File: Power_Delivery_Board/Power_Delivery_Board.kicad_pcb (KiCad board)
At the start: 2 copper layers, 36 parts, among them IC1 STUSB4500QTR, J1 USB C, J2 IO pins, J3 Power Output, J4 IO Pins, J5 Qwiic, Q1 STL6P3LLH6, SW1 SW_Push

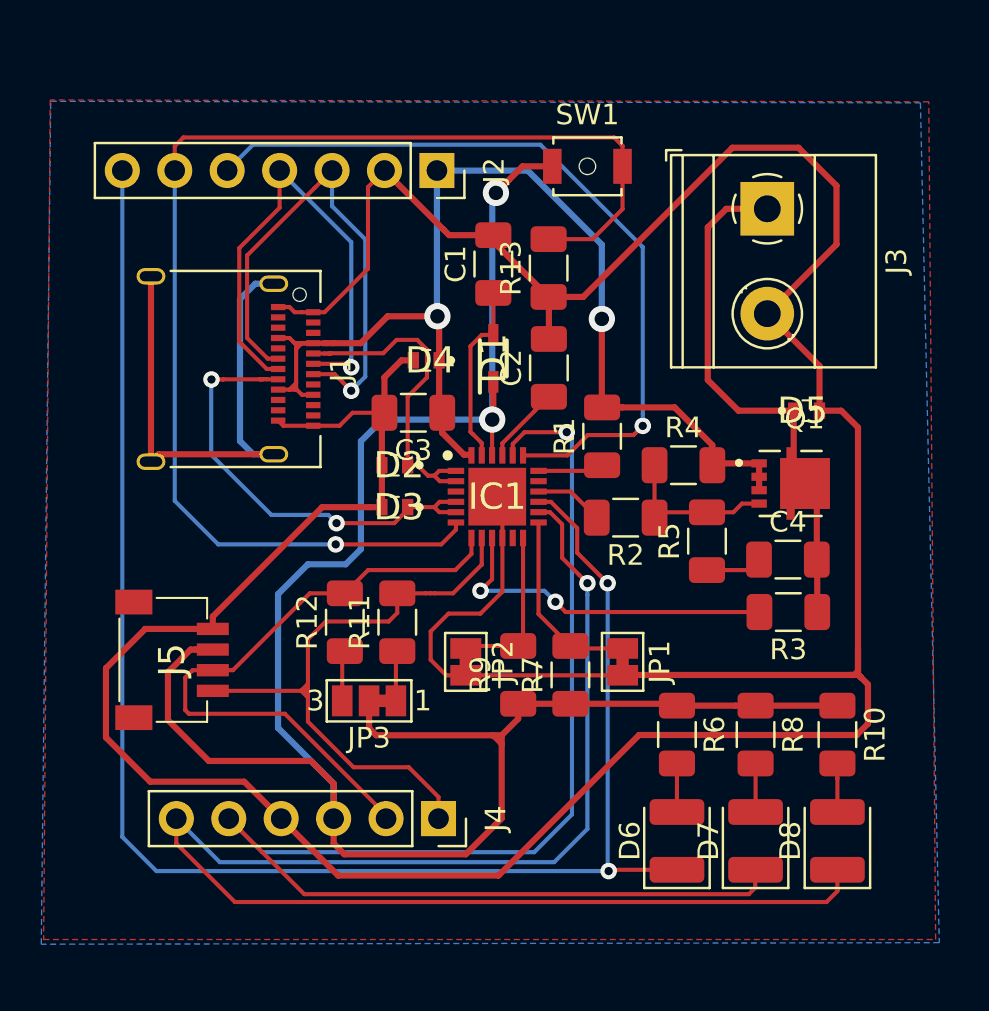
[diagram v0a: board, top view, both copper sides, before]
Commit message: Corrección de errores marcados por Fabiola
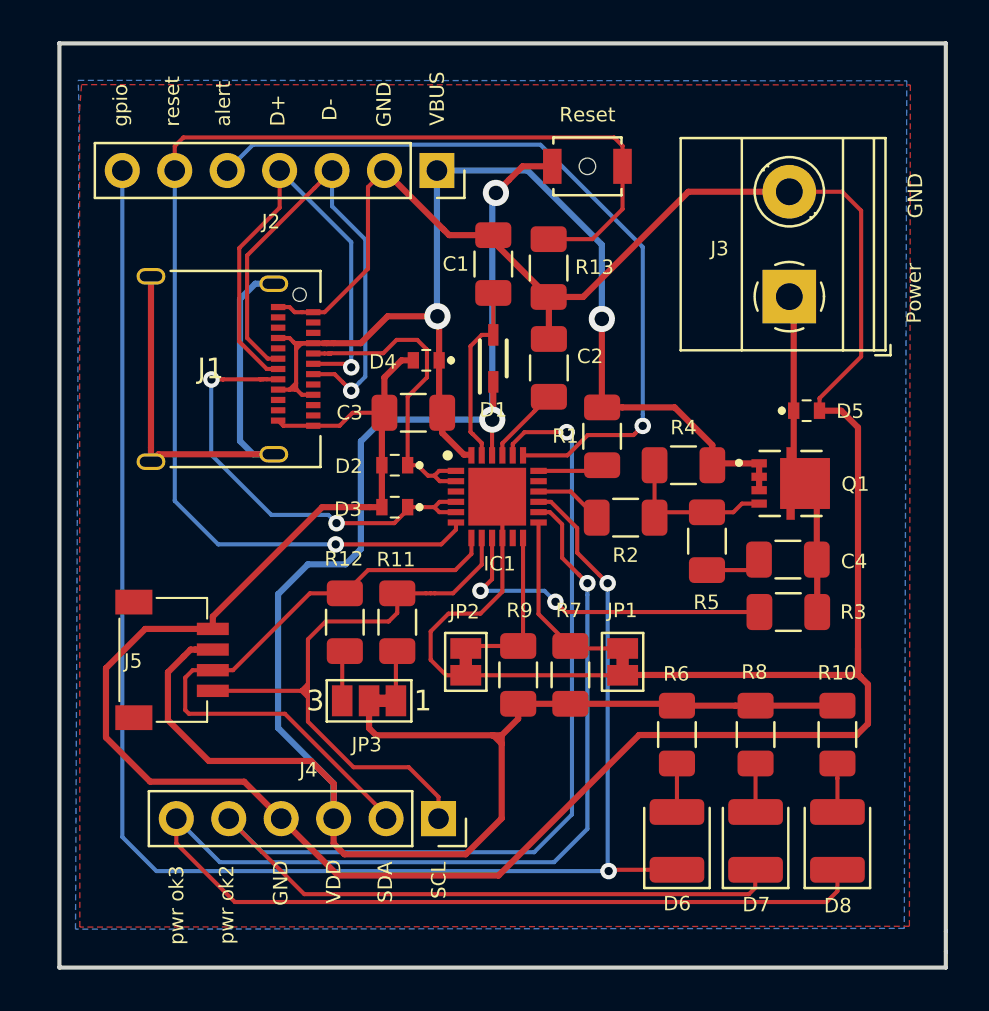
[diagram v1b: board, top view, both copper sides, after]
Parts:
- IC1: value STUSB4500QTR -> STUSB4500
- moved J3 4.39 mm to (168.6, 89.8), turned to 90 degrees
- renumbered SW1 to Reset
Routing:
- net power_output: track 25.7 -> 15.8 mm
- net GND: track 180.0 -> 177.2 mm
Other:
- board outline added: 43 x 44.8 mm
- board text added: "(por defecto) - pads 0.8mm - agujeros 0.4mm (VCC VDD GND) -pads 1.27 - agujeros 0.7mm"
- board text added: "D+"
- board text added: "D-"
- board text added: "GND"
- board text added: "Power"
- board text added: "SCL"
- board text added: "SDA"
- board text added: "Se utilizaron las capacidades del fabricante Ernesto Mayer (documentación en la raíz del proyecto)"
- board text added: "VBUS"
- board text added: "VDD"
- board text added: "alert"
- board text added: "gpio"
- board text added: "pistas (por defecto) - ancho 0.2mm -margen 0.18mm pistas (VCC VDD GND) - ancho 0.3mm -margen 0.3mm"
- board text added: "pwr ok2"
- board text added: "pwr ok3"
- board text added: "reset"

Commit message: Agrego un agujero para anclaje mecánico
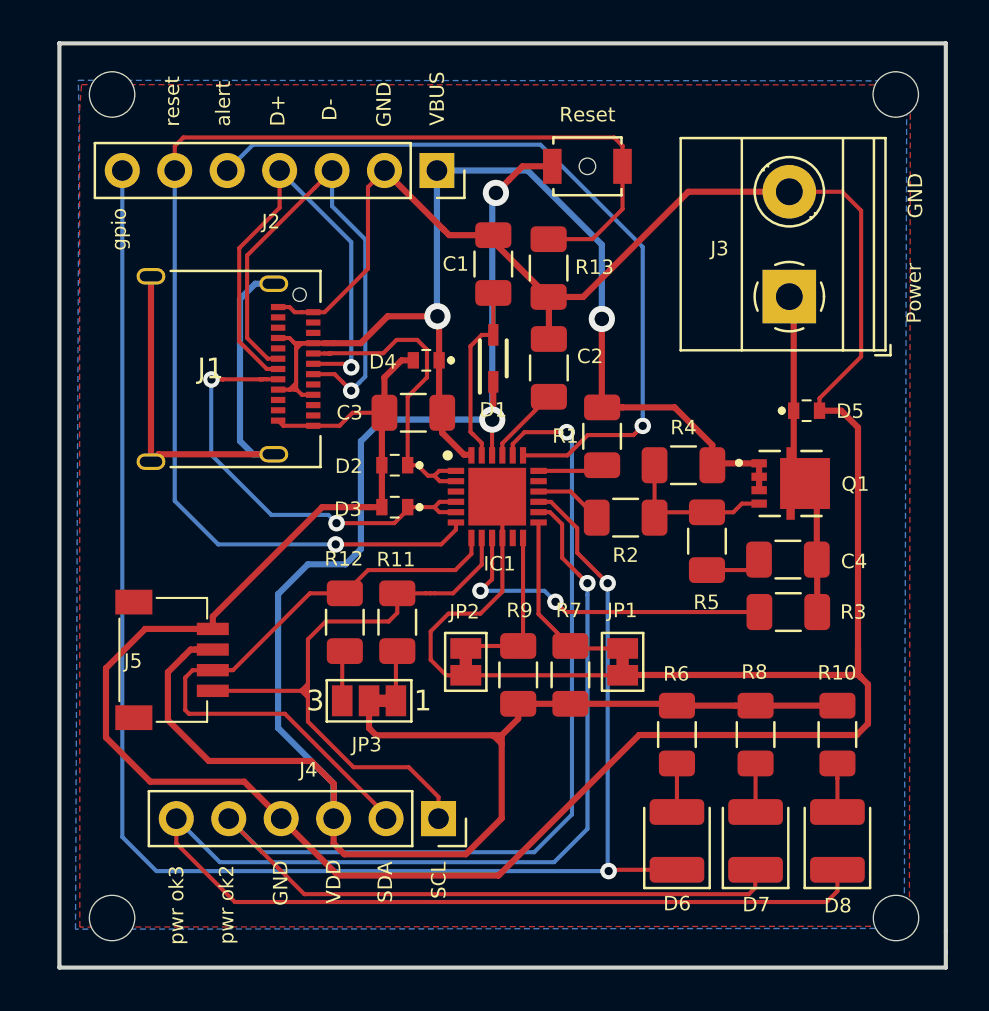
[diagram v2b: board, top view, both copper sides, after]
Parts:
- added REF**: MountingHole_2.2mm_M2_DIN965, MountingHole:MountingHole_2.2mm_M2_DIN965, F.Cu at (135.8, 119.9)
- added REF**: MountingHole_2.2mm_M2_DIN965, MountingHole:MountingHole_2.2mm_M2_DIN965, F.Cu at (173.8, 119.9)
- added REF**: MountingHole_2.2mm_M2_DIN965, MountingHole:MountingHole_2.2mm_M2_DIN965, F.Cu at (135.8, 80.0)
- added REF**: MountingHole_2.2mm_M2_DIN965, MountingHole:MountingHole_2.2mm_M2_DIN965, F.Cu at (173.8, 80.0)
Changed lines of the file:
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@@
     (tracks 412)
     (zones 0)
-    (modules 36)
+    (modules 40)
     (nets 38)
   )
@@
     )
   )
+  (module MountingHole:MountingHole_2.2mm_M2_DIN965 (layer F.Cu)
+    (at 135.8265 119.9134)
+    (descr "Mounting Hole 2.2mm, no annular, M2, DIN965")
+    (tags "mounting hole 2.2mm no annular m2 din965")
+    (attr virtual)
+    (fp_text reference REF** (at 0.1524 3.3274) (layer F.SilkS) hide
+      (effects (font (size 1 1) (thickness 0.15)))
+    )
+    (fp_text value MountingHole_2.2mm_M2_DIN965 (at 0 2.9) (layer F.Fab)
+      (effects (font (size 1 1) (thickness 0.15)))
+    )
+    (fp_circle (center 0 0) (end 2.15 0) (layer F.CrtYd) (width 0.05))
+    (fp_circle (center 0 0) (end 1.9 0) (layer Cmts.User) (width 0.15))
+    (fp_text user %R (at 0.3 0) (layer F.Fab)
+      (effects (font (size 1 1) (thickness 0.15)))
+    )
+    (pad 1 np_thru_hole circle (at 0 0) (size 2.2 2.2) (drill 2.2) (layers *.Cu *.Mask))
+  )
+  (module MountingHole:MountingHole_2.2mm_M2_DIN965 (layer F.Cu)
+    (at 173.7995 119.9134)
+    (descr "Mounting Hole 2.2mm, no annular, M2, DIN965")
+    (tags "mounting hole 2.2mm no annular m2 din965")
+    (attr virtual)
+    (fp_text reference REF** (at 0.4699 3.3401) (layer F.SilkS) hide
+      (effects (font (size 1 1) (thickness 0.15)))
+    )
+    (fp_text value MountingHole_2.2mm_M2_DIN965 (at 0 2.9) (layer F.Fab)
+      (effects (font (size 1 1) (thickness 0.15)))
+    )
+    (fp_circle (center 0 0) (end 2.15 0) (layer F.CrtYd) (width 0.05))
+    (fp_circle (center 0 0) (end 1.9 0) (layer Cmts.User) (width 0.15))
+    (fp_text user %R (at 0.3 0) (layer F.Fab)
+      (effects (font (size 1 1) (thickness 0.15)))
+    )
+    (pad 1 np_thru_hole circle (at 0 0) (size 2.2 2.2) (drill 2.2) (layers *.Cu *.Mask))
+  )
+  (module MountingHole:MountingHole_2.2mm_M2_DIN965 (layer F.Cu)
+    (at 135.8265 80.0227)
+    (descr "Mounting Hole 2.2mm, no annular, M2, DIN965")
+    (tags "mounting hole 2.2mm no annular m2 din965")
+    (attr virtual)
+    (fp_text reference REF** (at 0 -2.9) (layer F.SilkS) hide
+      (effects (font (size 1 1) (thickness 0.15)))
+    )
+    (fp_text value MountingHole_2.2mm_M2_DIN965 (at 0 2.9) (layer F.Fab)
+      (effects (font (size 1 1) (thickness 0.15)))
+    )
+    (fp_circle (center 0 0) (end 2.15 0) (layer F.CrtYd) (width 0.05))
+    (fp_circle (center 0 0) (end 1.9 0) (layer Cmts.User) (width 0.15))
+    (fp_text user %R (at 0.3 0) (layer F.Fab)
+      (effects (font (size 1 1) (thickness 0.15)))
+    )
+    (pad 1 np_thru_hole circle (at 0 0) (size 2.2 2.2) (drill 2.2) (layers *.Cu *.Mask))
+  )
+  (module MountingHole:MountingHole_2.2mm_M2_DIN965 (layer F.Cu)
+    (at 173.7868 80.0227)
+    (descr "Mounting Hole 2.2mm, no annular, M2, DIN965")
+    (tags "mounting hole 2.2mm no annular m2 din965")
+    (attr virtual)
+    (fp_text reference REF** (at 0 -2.9) (layer F.SilkS) hide
+      (effects (font (size 1 1) (thickness 0.15)))
+    )
+    (fp_text value MountingHole_2.2mm_M2_DIN965 (at 0 2.9) (layer F.Fab)
+      (effects (font (size 1 1) (thickness 0.15)))
+    )
+    (fp_circle (center 0 0) (end 2.15 0) (layer F.CrtYd) (width 0.05))
+    (fp_circle (center 0 0) (end 1.9 0) (layer Cmts.User) (width 0.15))
+    (fp_text user %R (at 0.3 0) (layer F.Fab)
+      (effects (font (size 1 1) (thickness 0.15)))
+    )
+    (pad 1 np_thru_hole circle (at 0 0) (size 2.2 2.2) (drill 2.2) (layers *.Cu *.Mask))
+  )
   (gr_line (start 134.1882 119.1387) (end 134.1882 120.3198) (layer Margin) (width 0.2))
   (gr_line (start 174.2821 120.3452) (end 174.2948 120.3579) (layer Margin) (width 0.2))
@@
     (effects (font (size 0.7 0.7) (thickness 0.1)))
   )
-  (gr_text gpio (at 136.2329 80.5434 90) (layer F.SilkS)
+  (gr_text gpio (at 136.1694 86.5505 90) (layer F.SilkS)
     (effects (font (size 0.7 0.7) (thickness 0.1)))
   )
